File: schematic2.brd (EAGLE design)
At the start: 92.7 x 53.3 mm, 70 parts, among them IC6 DS3231/SO

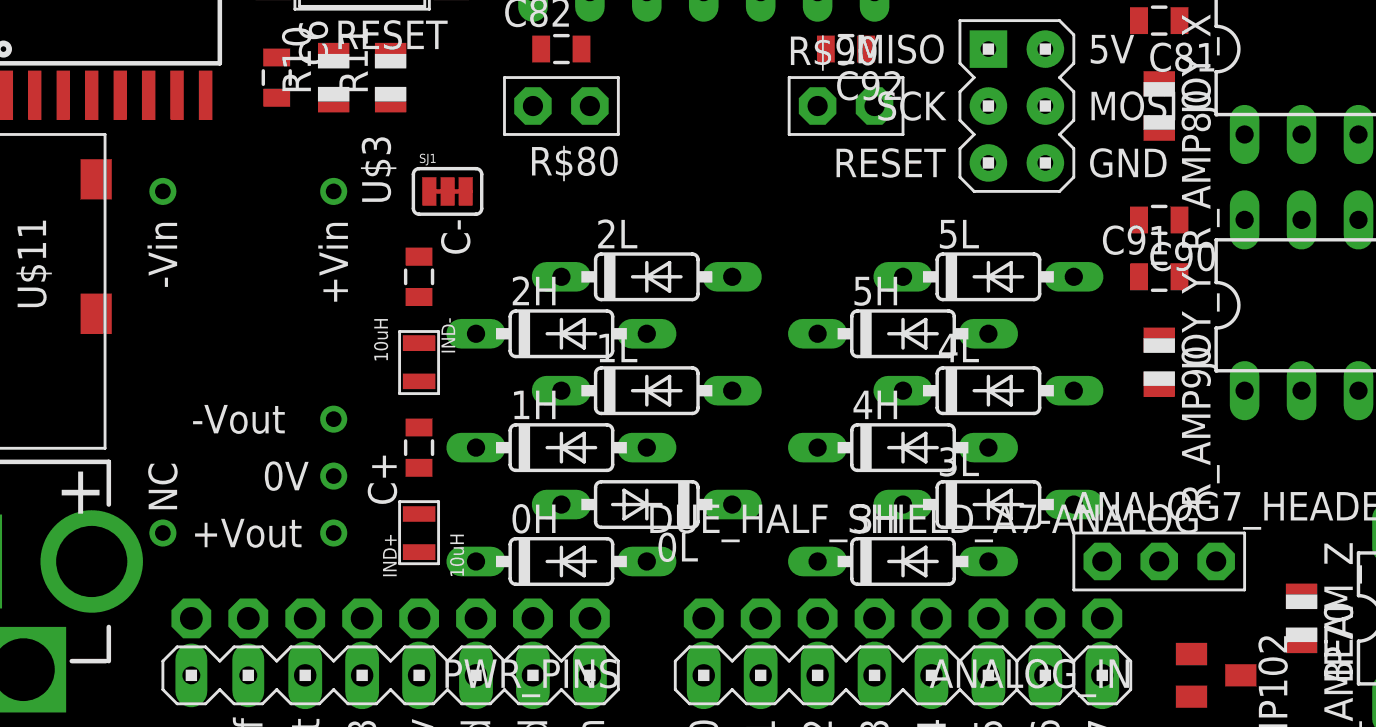
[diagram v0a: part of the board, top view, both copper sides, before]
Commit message: Found an unconnected wire on the schematic, moved some footprints around
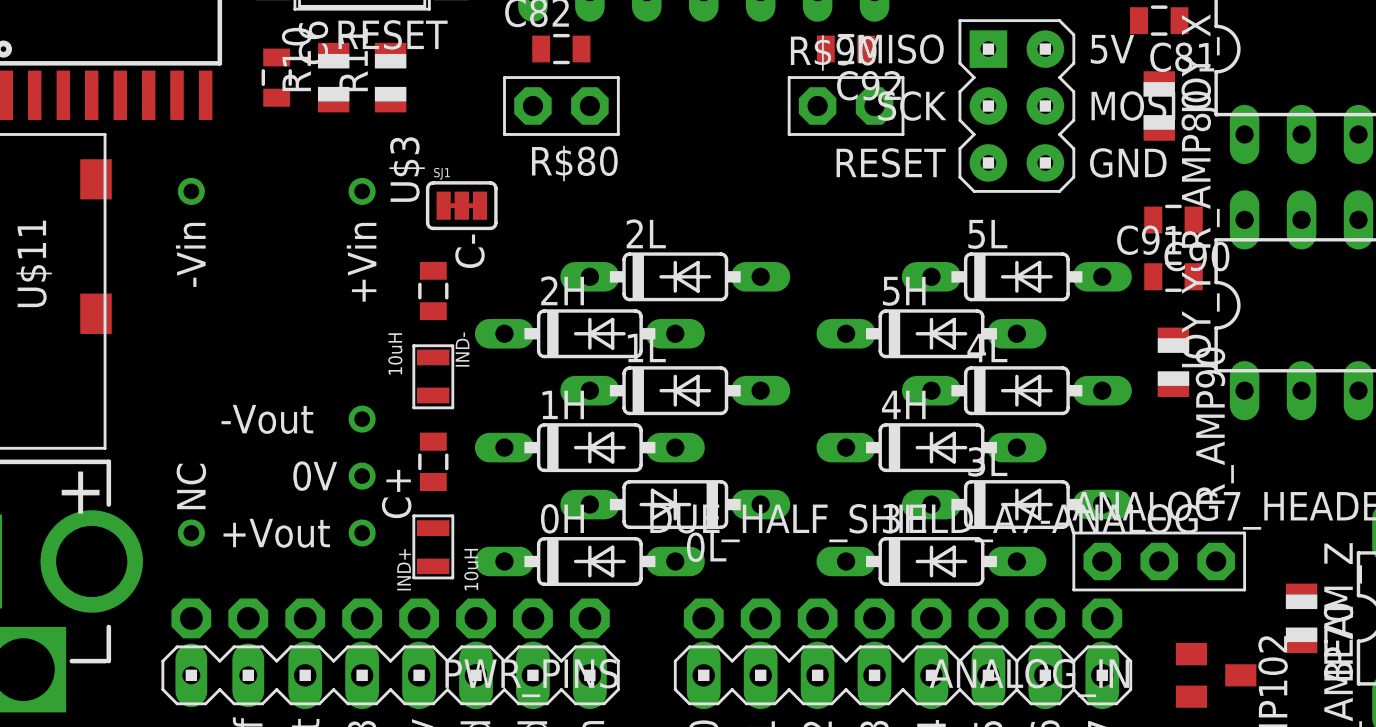
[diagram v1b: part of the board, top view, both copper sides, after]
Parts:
- moved 0L 1.27 mm to (40.6, 10.2)
- moved 1L 1.27 mm to (40.6, 15.2)
- moved 2L 1.27 mm to (40.6, 20.3)
- moved 3H 1.27 mm to (52.1, 7.62)
- moved 3L 1.27 mm to (55.9, 10.2)
- moved 4H 1.27 mm to (52.1, 12.7)
- moved 4L 1.27 mm to (55.9, 15.2)
- moved 5H 1.27 mm to (52.1, 17.8)
- moved 5L 1.27 mm to (55.9, 20.3)
- moved U$3 1.27 mm to (22.9, 16.5)
- moved 0H 1.27 mm to (36.8, 7.62)
- moved 1H 1.27 mm to (36.8, 12.7)
- moved 2H 1.27 mm to (36.8, 17.8)
- moved C- 0.90 mm to (29.8, 19.7)
- moved IND- 0.90 mm to (29.8, 15.9)
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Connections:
- net +3V3: now also 2H.C

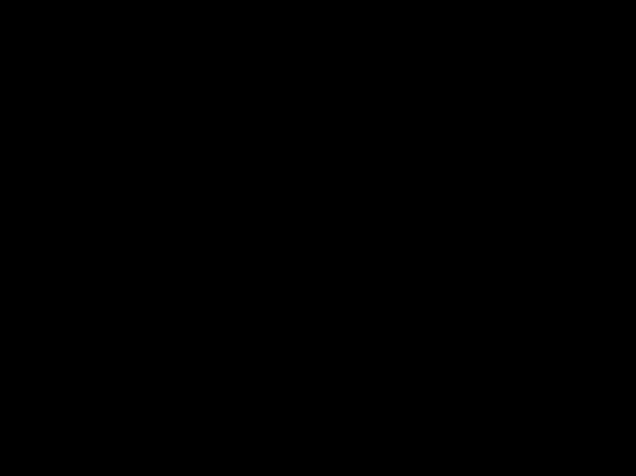
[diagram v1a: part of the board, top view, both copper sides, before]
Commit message: Added slide switch to schematic
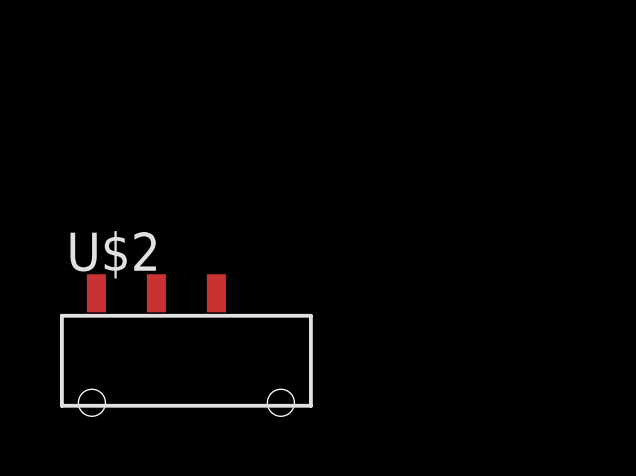
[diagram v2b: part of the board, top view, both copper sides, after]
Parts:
- added U$2: SWITCH_SLIDE_SMD_SPDT, Felicia_force_logger:SWITCH_SMD_RA_SPDT
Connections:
- new net VIN: U$1.VIN1, U$2.P$3_COMMON, U$3.P$14_VIN
- net VRAW: now also U$2.P$2; no longer U$1.VIN1, U$3.P$14_VIN
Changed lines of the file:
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@@
 <element name="BEAM" library="Felicia_force_logger" package="1X04_BIGLOCK" value="PINHD-1X4" x="88.9" y="17.78" rot="R90"/>
 <element name="IND+" library="Felicia_force_logger" package="I_0805" value="10uH" x="29.845" y="8.255" rot="R90"/>
+<element name="U$2" library="Felicia_force_logger" package="SWITCH_SMD_RA_SPDT" value="SWITCH_SLIDE_SMD_SPDT" x="-10.16" y="-13.97"/>
 </elements>
 <signals>
@@
 </signal>
 <signal name="VRAW">
-<contactref element="U$3" pad="P$14_VIN"/>
+<contactref element="PWR_PINS" pad="1"/>
 <contactref element="U$28" pad="P$1"/>
-<contactref element="U$1" pad="VIN1"/>
-<contactref element="PWR_PINS" pad="1"/>
-<wire x1="14.605" y1="7.62" x2="26.67" y2="24.13" width="0" layer="19" extent="1-1"/>
-<wire x1="36.83" y1="5.08" x2="26.67" y2="24.13" width="0" layer="19" extent="1-1"/>
-<wire x1="36.83" y1="2.54" x2="36.83" y2="5.08" width="0" layer="19" extent="1-1"/>
+<contactref element="U$2" pad="P$2"/>
+<wire x1="14.605" y1="7.62" x2="36.83" y2="5.08" width="0" layer="19" extent="1-1"/>
+<wire x1="-11.16" y1="-10.22" x2="14.605" y2="7.62" width="0" layer="19" extent="1-1"/>
 </signal>
 <signal name="-5V">
@@
 <wire x1="61.965" y1="20.32" x2="63.13" y2="31.75" width="0" layer="19" extent="1-1"/>
 </signal>
+<signal name="VIN">
+<contactref element="U$2" pad="P$3_COMMON"/>
+<contactref element="U$3" pad="P$14_VIN"/>
+<contactref element="U$1" pad="VIN1"/>
+<wire x1="36.83" y1="2.54" x2="26.67" y2="24.13" width="0" layer="19" extent="1-1"/>
+<wire x1="-9.16" y1="-10.22" x2="36.83" y2="2.54" width="0" layer="19" extent="1-1"/>
+</signal>
 </signals>

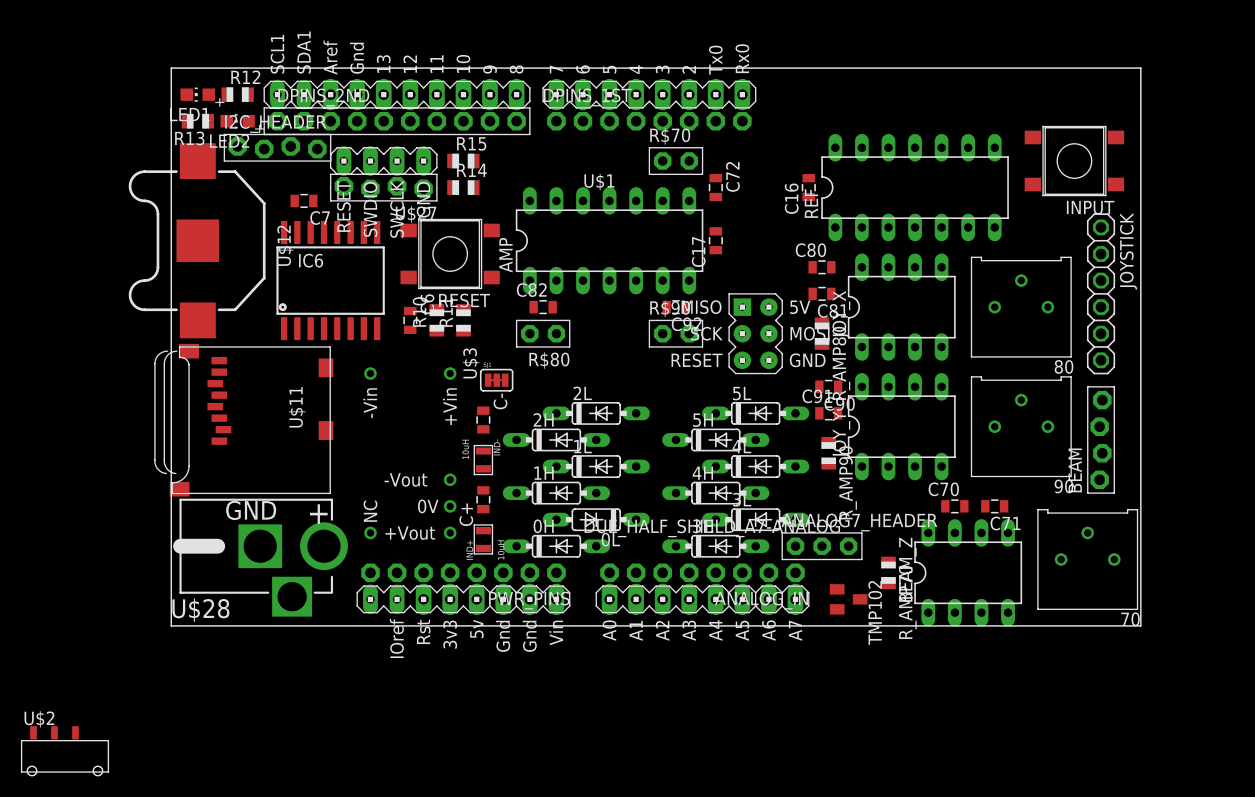
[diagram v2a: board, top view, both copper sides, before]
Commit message: Moved pieces around the board prior to drawing traces. Inserted the slide switch for raw voltage.
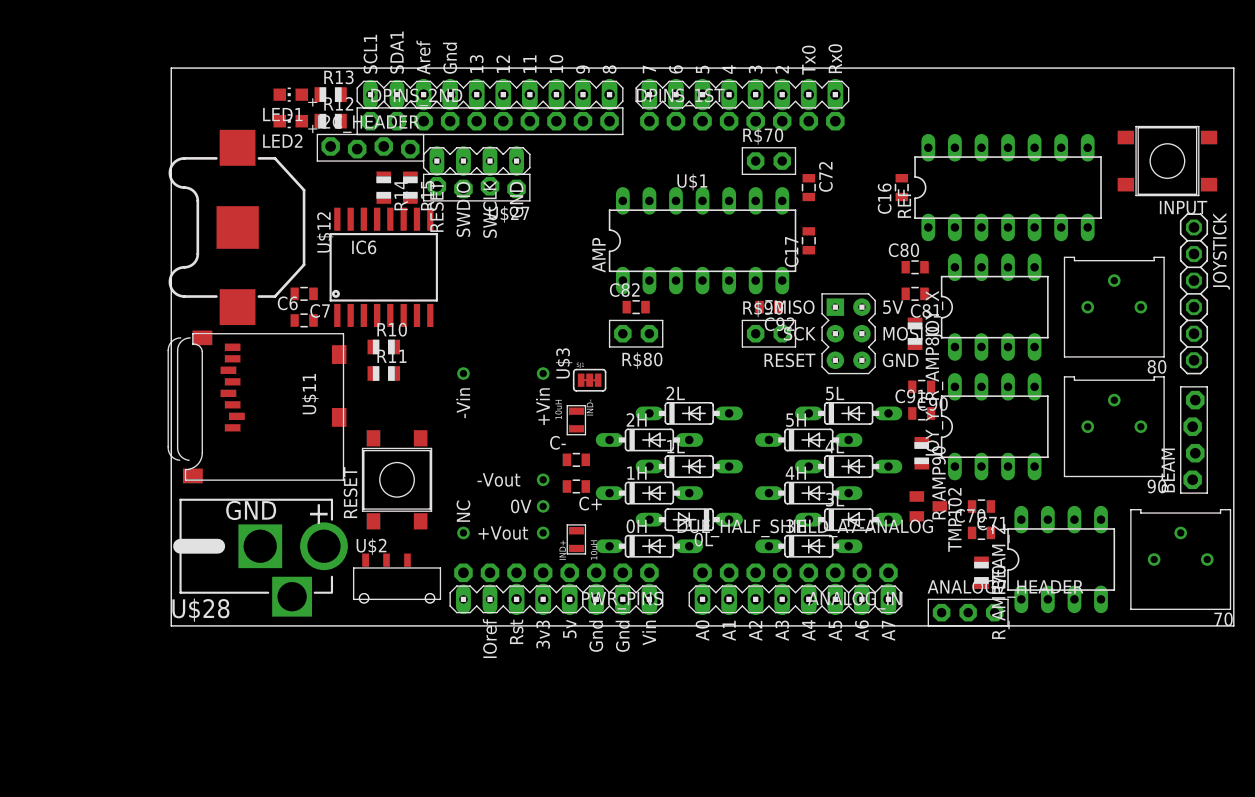
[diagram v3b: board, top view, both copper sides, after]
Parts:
- moved U$2 35.8 mm to (21.6, 2.54)
- moved RESET 22.2 mm to (21.6, 14.0), turned to 90 degrees
- moved ANALOG7_HEADER 15.3 mm to (76.2, 1.27)
- moved R13 13.0 mm to (15.2, 50.8), turned to 0 degrees
- moved TMP102 11.7 mm to (72.4, 11.4)
- moved C6 10.2 mm to (12.7, 29.2), turned to 0 degrees
- moved C- 9.67 mm to (38.7, 15.9), turned to 0 degrees
- moved IND- 9.67 mm to (38.7, 19.7)
- moved R12 9.25 mm to (15.2, 48.3)
- moved R11 9.16 mm to (20.3, 24.1), turned to 0 degrees
- moved BEAM_Z 8.98 mm to (85.1, 6.35)
- moved C+ 8.98 mm to (38.7, 13.3), turned to 180 degrees
- moved C80 8.89 mm to (71.1, 34.3)
- moved C81 8.89 mm to (71.1, 31.8)
- moved R_AMP80 8.89 mm to (71.1, 27.9)
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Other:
- board size 92.7 x 53.3 mm -> 101.6 x 53.3 mm

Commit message: Started initial routing. Swapped pins from the joystick input header to simplify routing to the in-amps.
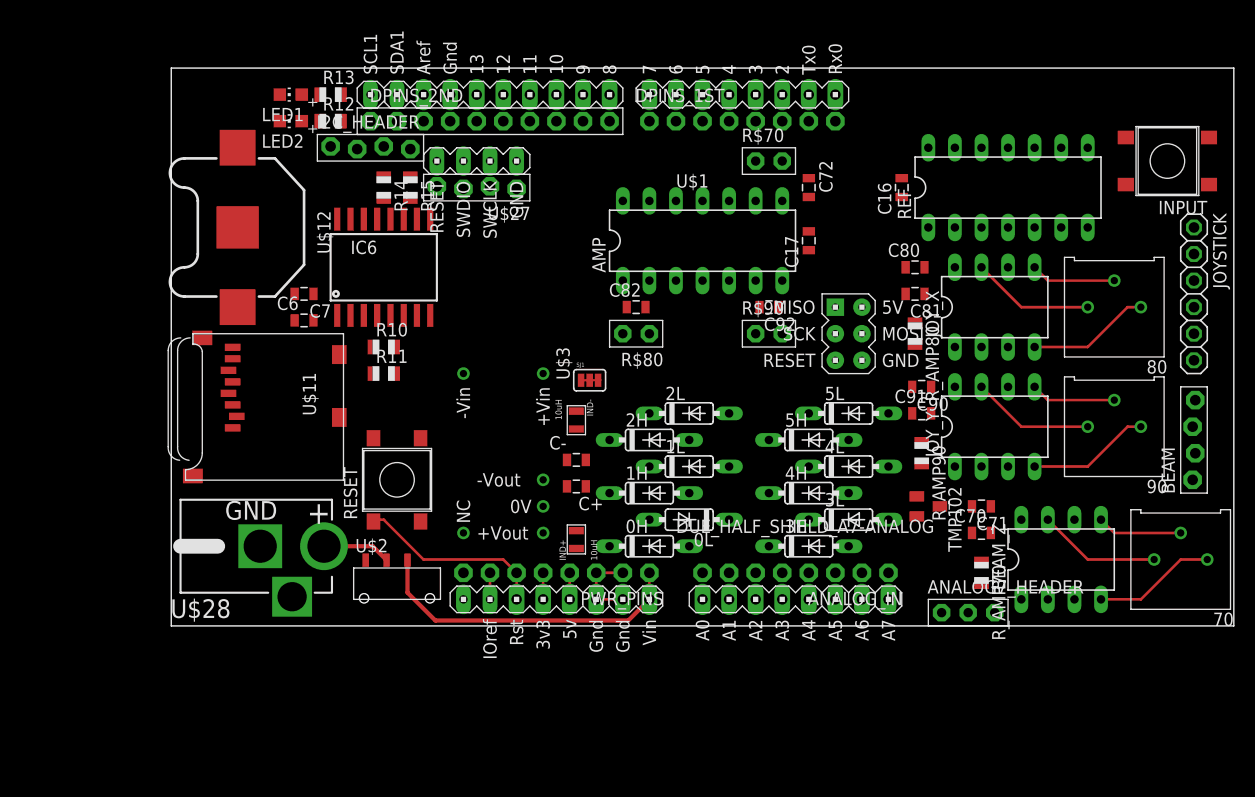
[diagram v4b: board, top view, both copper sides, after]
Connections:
- removed net 3V3: PWR_PINS.5
- removed net N$18: JOYSTICK.1, JOY_X.3
- removed net N$34: RESET.S$1, U$1.RESET
- new net N$1: JOYSTICK.2, JOY_X.3
- net +3V3: now also PWR_PINS.5
- net DGND: no longer U$1.GND_1, U$1.GND_2
- net GND: now also U$1.GND_1, U$1.GND_2
- net N$19: now also JOYSTICK.1; no longer JOYSTICK.2
- net N$23: now also JOY_Y.2; no longer JOY_Y.3
- net N$24: now also JOY_Y.3; no longer JOY_Y.2
- net RESET: now also RESET.S$1, U$1.RESET
- net VIN: now also PWR_PINS.1
- net VRAW: no longer PWR_PINS.1
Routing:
- net +5V: track 0.00 -> 35.2 mm
- net VNEG: track 0.00 -> 35.2 mm
- net VIN: track 0.00 -> 30.7 mm
- net RESET: track 0.00 -> 18.4 mm
- net A4: track 0.00 -> 8.15 mm
- net A3: track 0.00 -> 8.15 mm
- net A5: track 0.00 -> 8.15 mm
- net GND: track 0.00 -> 7.62 mm
- net VRAW: track 0.00 -> 6.54 mm
- net IOREF: track 0.00 -> 2.54 mm
- net 5V: track 0.00 -> 2.54 mm
- net +3V3: track 0.00 -> 2.54 mm
